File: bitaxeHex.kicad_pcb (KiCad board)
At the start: 4 copper layers, 84.5 x 129.5 mm, 370 parts, among them J1 Conn_01x01, J2 Conn_01x01, J3 Conn_02x05_Odd_Even, J4 TC2030-IDC, J5 Conn_01x04, J6 Conn_01x06, J7 USB_C_Receptacle_USB2.0, J8 Conn_01x04, J9 Conn_01x04, SW1 SWITCH-SPST, SW2 SWITCH-SPST, U1 LMR54410, U10 AP7331, U11 AP7331, U12 BM1368_mode1, U13 BM1368_mode0, U14 25MHz, U15 TLV3544, U16 AP7331, U17 AP7331, U18 BM1368_mode0, U19 25MHz, U2 RT9080-33GJ5, U21 TLV3544, U23 AP7331, U24 AP7331, U25 BM1368_mode1, U26 25MHz, U27 BM1368_mode1, U28 BM1368_mode1, U3 TPS546D24ARVFR, U4 MIC5504-MS, U5 SN74AVC4T774, U6 ESP32-S3-WROOM-1, U7 TMP1075, U8 TMP1075, U9 EMC2302, Y1 32.768kHz

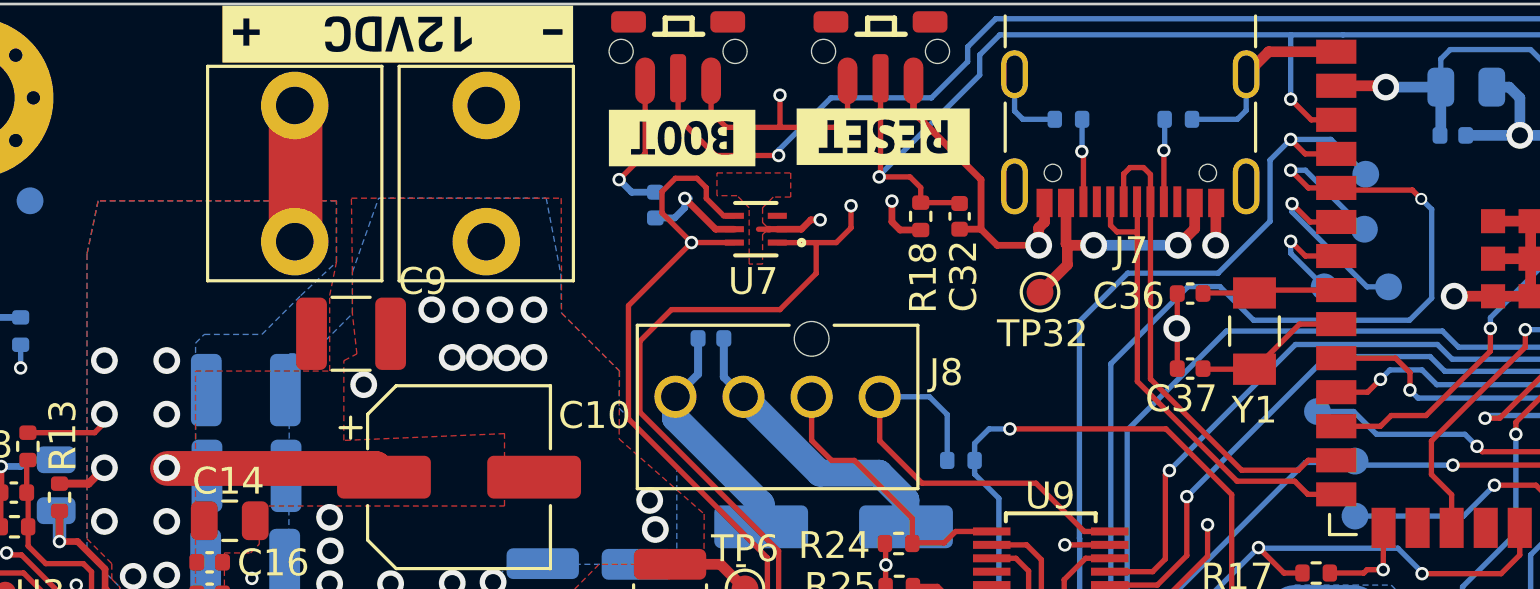
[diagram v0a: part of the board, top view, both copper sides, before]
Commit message: -Reset to 1V8/0V8 setup -Add TVS protection
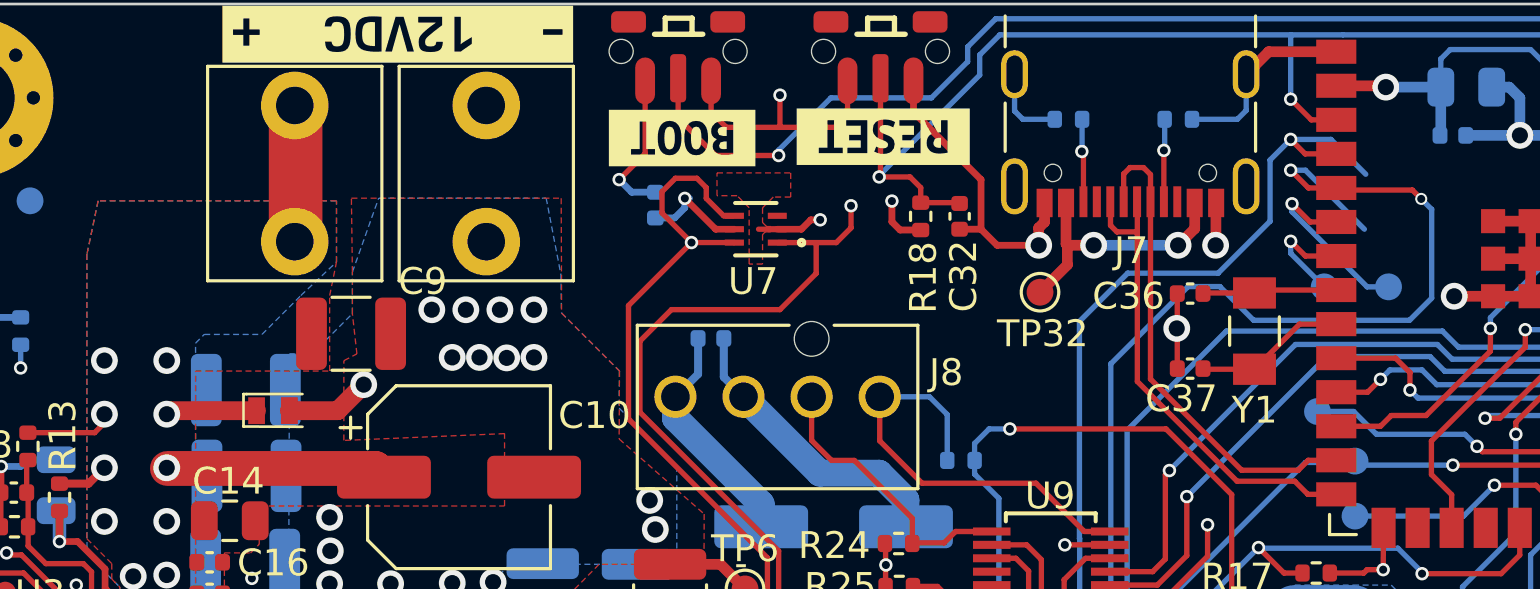
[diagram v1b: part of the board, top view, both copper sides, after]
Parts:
- removed TP12, TP13: TestPoint, TestPoint:TestPoint_Pad_D1.0mm
- added D1: 824045812, bitaxe:824045812, F.Cu at (64.7, 61.2)
- R30, R38, R64: value 110k -> 115k
- R32, R40, R66: value 220k -> 402k
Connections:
- net /BM1368-1/1V2 renamed /BM1368-1/1V8
- net /BM1368-2/1V2 renamed /BM1368-2/1V8
- net /BM1368-3/1V2 renamed /BM1368-3/1V8
- C25 pad 1: /1V2 -> /1V8
- C34 pad 2: /1V2 -> /ESP32/1V8
- C47 pad 1: BM1368-1/0V8 -> Net-(U28-VDDIO_08_0)
- C53 pad 1: BM1368-1/0V8 -> GND
- C58 pad 1: BM1368-1/0V8 -> GND
- C67 pad 1: BM1368-1/0V8 -> GND
- C76 pad 1: BM1368-1/0V8 -> GND
- R31 pad 2: BM1368-1/0V8 -> GND
- TP35 pad 1: BM1368-1/0V8 -> GND
- TP4 pad 1: /1V2 -> /1V8
- U10 pad 5: BM1368-1/0V8 -> GND
- U12 pad 14: BM1368-1/0V8 -> GND
- U12 pad 17: BM1368-1/0V8 -> GND
- U28 pad 14: BM1368-1/0V8 -> Net-(U28-VDDIO_08_0)
- U28 pad 17: BM1368-1/0V8 -> GND
- U4 pad 5: /1V2 -> /1V8
- U5 pad 16: /1V2 -> /ESP32/1V8
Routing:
- net GND: track 374.0 -> 446.6 mm, vias 110 -> 114
- net BM1368-1/0V8: track 69.4 -> 0.00 mm, vias 4 -> 0
- net /1V8: track 0.00 -> 16.2 mm
- net /1V2: track 16.2 -> 0.00 mm
- net /VIN: track 111.7 -> 115.1 mm
